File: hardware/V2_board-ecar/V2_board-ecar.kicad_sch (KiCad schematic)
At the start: 80 parts, among them IC1 ATMEGA8A-P, J1 2x BATT IN, J10 24V, J11 18V, J12 5V, J13 Analog-in-3 - 30to5 (batt), J14 Screw_Terminal_01x03, J15 Gas Pedal, J2 2x 24V filtered, J3 ST 2x GND, J4 ST 2x GND, J5 IGBT, J6 LED ~3,2V 20mA, J7 Analog-in-2 0-5V, J8 2x Mosfet OUT, J9 BATT, K1 LEG-5, P1 ISP, Q1 IRFZ24N, Q2 IRFZ24N, Q3 BC547, Q4 BC547, U1 LM2576T-5, U2 LM7818CT, U4 TC429

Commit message: pcb: Add 2x switch input, split into 3 sheets, remove mosfet output
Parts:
- removed BZ1: Buzzer, symbol Device:Buzzer
- removed C1, C2: 2200uf, symbol Device:C_Polarized
- removed C10: 100nF, ~, symbol treiber-rescue:C
- removed C11: 100n, ~, symbol treiber-rescue:C
- removed C12: 10uF, ~, symbol treiber-rescue:C
- removed C15: 10u, symbol Device:C
- removed C16, C19, C3: 100n, symbol Device:C
- removed C17: 100uF, ~, symbol treiber-rescue:C
- removed C4: 1000u, symbol Device:C_Polarized
- removed C5: 100u, symbol Device:C_Polarized
- removed C9: 330nF, ~, symbol treiber-rescue:C
- removed D1, D10, D11, D12, D13, D14, D15, D4: D, symbol Device:D
- removed D17, D7, D9: 5V1, symbol Device:D_Zener
- removed D2: TVS 26V (starts 31V), Diode_THT:D_DO-201AE_P15.24mm_Horizontal, symbol Diode:1.5KExxCA
- removed D3: 1N5822, Diode_THT:D_DO-201AD_P15.24mm_Horizontal, symbol Diode:1N5822
- removed D5: LED 3mm green 20mA 2.5V, ~, symbol control-rescue:LED
- removed F1: 500mA, symbol Device:Fuse
- removed J1: 2x BATT IN, symbol Connector:Screw_Terminal_01x02
- removed J10: 24V, symbol Connector:Conn_01x01_Pin
- removed J11: 18V, symbol Connector:Conn_01x01_Pin
- removed J12: 5V, symbol Connector:Conn_01x01_Pin
- removed J13: Analog-in-3 - 30to5 (batt), symbol Connector:Screw_Terminal_01x02
- removed J14: Screw_Terminal_01x03, symbol Connector:Screw_Terminal_01x03
- removed J15: Gas Pedal, symbol Connector:Screw_Terminal_01x03
- removed J2: 2x 24V filtered, symbol Connector:Screw_Terminal_01x02
- removed J3, J4: ST 2x GND, symbol Connector:Screw_Terminal_01x02
- removed J5: IGBT, symbol Connector:Screw_Terminal_01x02
- removed J6: LED ~3,2V 20mA, symbol Connector:Screw_Terminal_01x02
- removed J7: Analog-in-2 0-5V, symbol Connector:Screw_Terminal_01x02
- removed J8: 2x Mosfet OUT, symbol Connector:Screw_Terminal_01x02
- removed J9: BATT, symbol Connector:Conn_01x01_Pin
- removed K1: LEG-5, Relay_THT:Relay_SPDT_SANYOU_SRD_Series_Form_C, symbol Relay:SANYOU_SRD_Form_C
- removed L2: 100u, symbol Device:L
- removed OC1: LTV-817, Package_DIP_AKL:DIP-4_W7.62mm_LongPads, symbol Optocoupler_AKL:LTV-817
- removed Q1, Q2: IRFZ24N, Package_TO_SOT_THT_AKL:TO-220-3_Vertical_GDS, symbol Transistor_MOSFET_AKL:IRFZ24N
- removed Q3, Q4: BC547, Package_TO_SOT_THT_AKL:TO-92_Inline_Wide_CBE, symbol Transistor_BJT_AKL:BC547
- removed R1, R2: 2.5, symbol Device:R
- removed R10: 150k, ~, symbol control-rescue:R
- removed R11: 30k, ~, symbol control-rescue:R
- removed R12, R13, R18: 1k, ~, symbol control-rescue:R
- removed R14, R16: 1k, symbol Device:R
- removed R15, R17: 22k, symbol Device:R
- removed R19, R21: 470, symbol Device:R
- removed R20: 100, symbol Device:R
- removed R3: nopop, symbol Device:R
- removed R5: 12k, ~, symbol treiber-rescue:R
- removed R6: 0, ~, symbol treiber-rescue:R
- removed R7: 4k7, ~, symbol treiber-rescue:R
- removed R8: 320, ~, symbol treiber-rescue:R
- removed R9: 130, ~, symbol control-rescue:R
- removed U1: LM2576T-5, Package_TO_SOT_THT:TO-220-5_Vertical, symbol Regulator_Switching:LM2576T-5
- removed U2: LM7818CT, TO-220, symbol treiber-rescue:LM7818CT
- removed U4: TC429, ~, symbol mcp1407:MCP1407
- R4: value R -> 10k
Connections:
- net LED-ext: now reaches IC1.28 ((ADC5/SCL)PC5)
- net OUT0 renamed Mosfet-fan
- net OUT1 renamed Relay-light
- net SW0 renamed Switch2
- net SW1 renamed Switch1
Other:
- added sheet Input-Output (board-ecar_IO.kicad_sch)
- added sheet Voltage-Supplies (supply.kicad_sch)
- note removed: "3A overcurrent safe"
- note removed: "7-40V"
- note removed: "Onboard Buzzer, LED"
- note removed: "Relay for Light"
- note removed: "TODO: measure gas pedal voltage-drivider resistance -> choose R high enough"
- note removed: "populate diodes depending on where load is connected"
- moved on the sheet: C6, C7, C8, IC1, P1, R4

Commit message: pcb: change to A3 sheet, re-arrange, minor optimizations
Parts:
- added BZ1: Buzzer, symbol Device:Buzzer
- added C1: 100u, symbol Device:C_Polarized
- added C10, C15, C16, C17, C18: 100n, symbol Device:C
- added C11: 10u, symbol Device:C
- added C12: 100n, ~, symbol treiber-rescue:C
- added C13: 10uF, ~, symbol treiber-rescue:C
- added C14: 100uF, ~, symbol treiber-rescue:C
- added C19, C5: 1000u, symbol Device:C_Polarized
- added C2: 330nF, ~, symbol treiber-rescue:C
- added C3: 100nF, ~, symbol treiber-rescue:C
- added C4, C9: 2200uf, symbol Device:C_Polarized
- added D1, D10, D11, D8, D9: D, symbol Device:D
- added D12, D13, D5, D6, D7: 5V1, symbol Device:D_Zener
- added D2: 1N5822, Diode_THT:D_DO-201AD_P15.24mm_Horizontal, symbol Diode:1N5822
- added D3: TVS 26V (starts 31V), Diode_THT:D_DO-201AE_P15.24mm_Horizontal, symbol Diode:1.5KExxCA
- added D4: LED 3mm green 20mA 2.5V, ~, symbol control-rescue:LED
- added F1: 500mA, symbol Device:Fuse
- added J1: 2x BATT IN, symbol Connector:Screw_Terminal_01x02
- added J10: 24V, symbol Connector:Conn_01x01_Pin
- added J11: 18V, symbol Connector:Conn_01x01_Pin
- added J12: 5V, symbol Connector:Conn_01x01_Pin
- added J13: Analog-in-2 0-5V, symbol Connector:Screw_Terminal_01x02
- added J14: IGBT, symbol Connector:Screw_Terminal_01x02
- added J15: Analog-in-3 - 30to5 (batt), symbol Connector:Screw_Terminal_01x02
- added J16: Mosfet Out (Fan), symbol Connector:Screw_Terminal_01x02
- added J17: 2x Switch (to 5V), symbol Connector:Screw_Terminal_01x02
- added J18: Relay contacts, symbol Connector:Screw_Terminal_01x03
- added J2, J4: ST 2x GND, symbol Connector:Screw_Terminal_01x02
- added J3: 2x 24V filtered, symbol Connector:Screw_Terminal_01x02
- added J5: PWM-Signal, symbol Connector:Conn_01x01_Pin
- added J6: LED ~3,2V 20mA, symbol Connector:Screw_Terminal_01x02
- added J7: Gas Pedal, symbol Connector:Screw_Terminal_01x03
- added J8: Gate, symbol Connector:Conn_01x01_Pin
- added J9: BATT, symbol Connector:Conn_01x01_Pin
- added K1: LEG-5, Relay_THT:Relay_SPDT_SANYOU_SRD_Series_Form_C, symbol Relay:SANYOU_SRD_Form_C
- added L1: 100u, symbol Device:L
- added OC1: LTV-817, Package_DIP_AKL:DIP-4_W7.62mm_LongPads, symbol Optocoupler_AKL:LTV-817
- added Q1, Q3: BC547, Package_TO_SOT_THT_AKL:TO-92_Inline_Wide_CBE, symbol Transistor_BJT_AKL:BC547
- added Q2: IRFZ24N, Package_TO_SOT_THT_AKL:TO-220-3_Vertical_GDS, symbol Transistor_MOSFET_AKL:IRFZ24N
- added R1, R3: 2.5, symbol Device:R
- added R10: 4k7, ~, symbol treiber-rescue:R
- added R11, R12, R20, R26, R27: 2k2, ~, symbol control-rescue:R
- added R13, R14: 1k, ~, symbol control-rescue:R
- added R16: 150k, ~, symbol control-rescue:R
- added R17: 30k, ~, symbol control-rescue:R
- added R18: 1k, symbol Device:R
- added R19: 22k, symbol Device:R
- added R2: nopop, symbol Device:R
- added R21, R5: 470, symbol Device:R
- added R22, R23, R24, R25: 10k, ~, symbol control-rescue:R
- added R6: 320, ~, symbol treiber-rescue:R
- added R7: 130, ~, symbol control-rescue:R
- added R8: 100, symbol Device:R
- added R9: 12k, ~, symbol treiber-rescue:R
- added U1: LM7818CT, TO-220, symbol treiber-rescue:LM7818CT
- added U2: LM2576T-5, Package_TO_SOT_THT:TO-220-5_Vertical, symbol Regulator_Switching:LM2576T-5
- added U3: TC429, ~, symbol mcp1407:MCP1407
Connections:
- net SPEED0 is gone; now on net Switch2: IC1.5 ((INT1)PD3)
- net SPEED1 is gone; now on net Switch1: IC1.4 ((INT0)PD2)
- net +5V: now also C5.1, D11.1 (K), D8.1 (K), J12.1 (Pin_1), J13.2 (Pin_2), J6.1 (Pin_1), J7.3 (Pin_3), K1.5, L1.2, U2.4 (FB)
- net BUZZER: now also BZ1.1 (+)
- net GND: now also BZ1.2 (-), C1.2, C10.2, C11.2, C12.2, C13.2, C14.2, C15.2, C16.2, C17.2, C18.2, C19.2, C2.2, C3.2, C4.2, C5.2, C9.2, D1.2 (A), D12.2 (A), D13.2 (A), D2.2 (A), D3.1 (A1), D4.2 (K), D5.2 (A), D6.2 (A), D7.2 (A), J14.2 (Pin_2), J2.1 (Pin_1), J2.2 (Pin_2), J4.1 (Pin_1), J4.2 (Pin_2), J7.1 (Pin_1), OC1.2, OC1.3, Q1.3 (E), Q2.3 (S), Q3.3 (E), R10.2, R17.2, R19.1, R22.2, R23.2, U1.2 (GND), U2.3 (GND), U2.5 (~{ON}/OFF), U3.4 (GND), U3.5 (GND)
- net LED: now also R7.2
- net LED-ext: now also R5.1
- net PWM_0: now also J5.1 (Pin_1), R6.1
- net Switch1: now also R26.2; no longer IC1.12 ((AIN0)PD6)
- net Switch2: now also R27.2; no longer IC1.13 ((AIN1)PD7)
- net analog1: now also R12.1
- net Mosfet-fan renamed Mosfet (fan)
- net Mosfet (fan): now also R18.2
- net PWM_1: no longer names the net of IC1.16 ((~{SS}/OC1B)PB2)
- net RX: no longer names the net of IC1.2 ((RXD)PD0)
- net Relay-light renamed Relay (light)
- net Relay (light): now also R21.1
- net TX: no longer names the net of IC1.3 ((TXD)PD1)
- net analog0 renamed analog0 (gas)
- net analog0 (gas): now also R11.1
- net analog2-30V renamed analog2 (30V Batt)
- net analog2 (30V Batt): now also R20.2
- new net: J15.1 (Pin_1), R16.1
- new net: C16.1, D7.1 (K), R16.2, R17.1, R20.1
- new net: F1.2, R1.1, R2.1
- new net: D4.1 (A), R7.1
- new net: J14.1 (Pin_1), J8.1 (Pin_1), U3.6 (OUT), U3.7 (OUT)
- new net: D10.2 (A), D8.2 (A), D9.2 (A), J16.1 (Pin_1), Q2.2 (D)
- new net: C11.1, D5.1 (K), R11.2, R13.2
- new net: J13.1 (Pin_1), R14.1
- new net: C15.1, D6.1 (K), R12.2, R14.2
- new net: C18.1, D13.1 (K), R25.2, R27.1
- new net: Q1.1 (C), R8.2
- new net: Q1.2 (B), R5.2
- new net: Q3.2 (B), R21.2
- new net: R1.2, R3.1
- new net: Q2.1 (G), R18.1, R19.2
- new net: J7.2 (Pin_2), R13.1
- new net: J6.2 (Pin_2), R8.1
- new net: J17.1 (Pin_1), R22.1, R24.1
- new net: J17.2 (Pin_2), R23.1, R25.1
- new net: J18.1 (Pin_1), K1.4
- new net: J18.2 (Pin_2), K1.1
- new net: J18.3 (Pin_3), K1.3
- new net: D11.2 (A), K1.2, Q3.1 (C)
- new net: C17.1, D12.1 (K), R24.2, R26.1
- new net: OC1.1, R6.2
- new net: OC1.4, R10.1, R9.2, U3.2 (INPUT)
- new net: D2.1 (K), L1.1, U2.2 (OUT)
- new net +18V: C12.1, C13.1, C14.1, C19.1, C3.1, J11.1 (Pin_1), R9.1, U1.3 (OUT), U3.1 (Vdd), U3.8 (Vdd)
- new net +24V filtered: C1.1, C10.1, C2.1, C4.1, C9.1, D1.1 (K), D3.2 (A2), D9.1 (K), J10.1 (Pin_1), J15.2 (Pin_2), J16.2 (Pin_2), J3.1 (Pin_1), J3.2 (Pin_2), R2.2, R3.2, U1.1 (IN), U2.1 (VIN)
- new net +BATT: D10.1 (K), F1.1, J1.1 (Pin_1), J1.2 (Pin_2), J9.1 (Pin_1)
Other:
- removed sheet Input-Output
- removed sheet Voltage-Supplies
- note added: "18V Supply (linear regulator)"
- note added: "18V needed for mosfet driver"
- note added: "24V Supply voltage filter"
- note added: "2x Digital input (Switches to 5V)"
- note added: "3A overcurrent safe"
- note added: "5V Supply (buck converter)"
- note added: "7-40V"
- note added: "ADC Battery voltage"
- note added: "ADC Gas pedal"
- note added: "ADC Reserve"
- note added: "Filter 50V peaks on battery voltage each pwm cycle"
- note added: "Mosfet driver for IGBT"
- note added: "Mosfet out (cooling Fan)"
- note added: "Onboard Buzzer and LED"
- note added: "Relay for Light"
- note added: "TODO: measure gas pedal voltage-drivider resistance -> choose R high enough"
- note added: "external LED"
- note added: "populate diodes depending on where load is connected"
- note added: "test pins supplies"
- note removed: "Shopping list: 5V Voltage regulator LM2576T-5 Diode 1N5822 100uH >3A inductor"
- moved on the sheet: C6, C7, C8, IC1, P1, R4

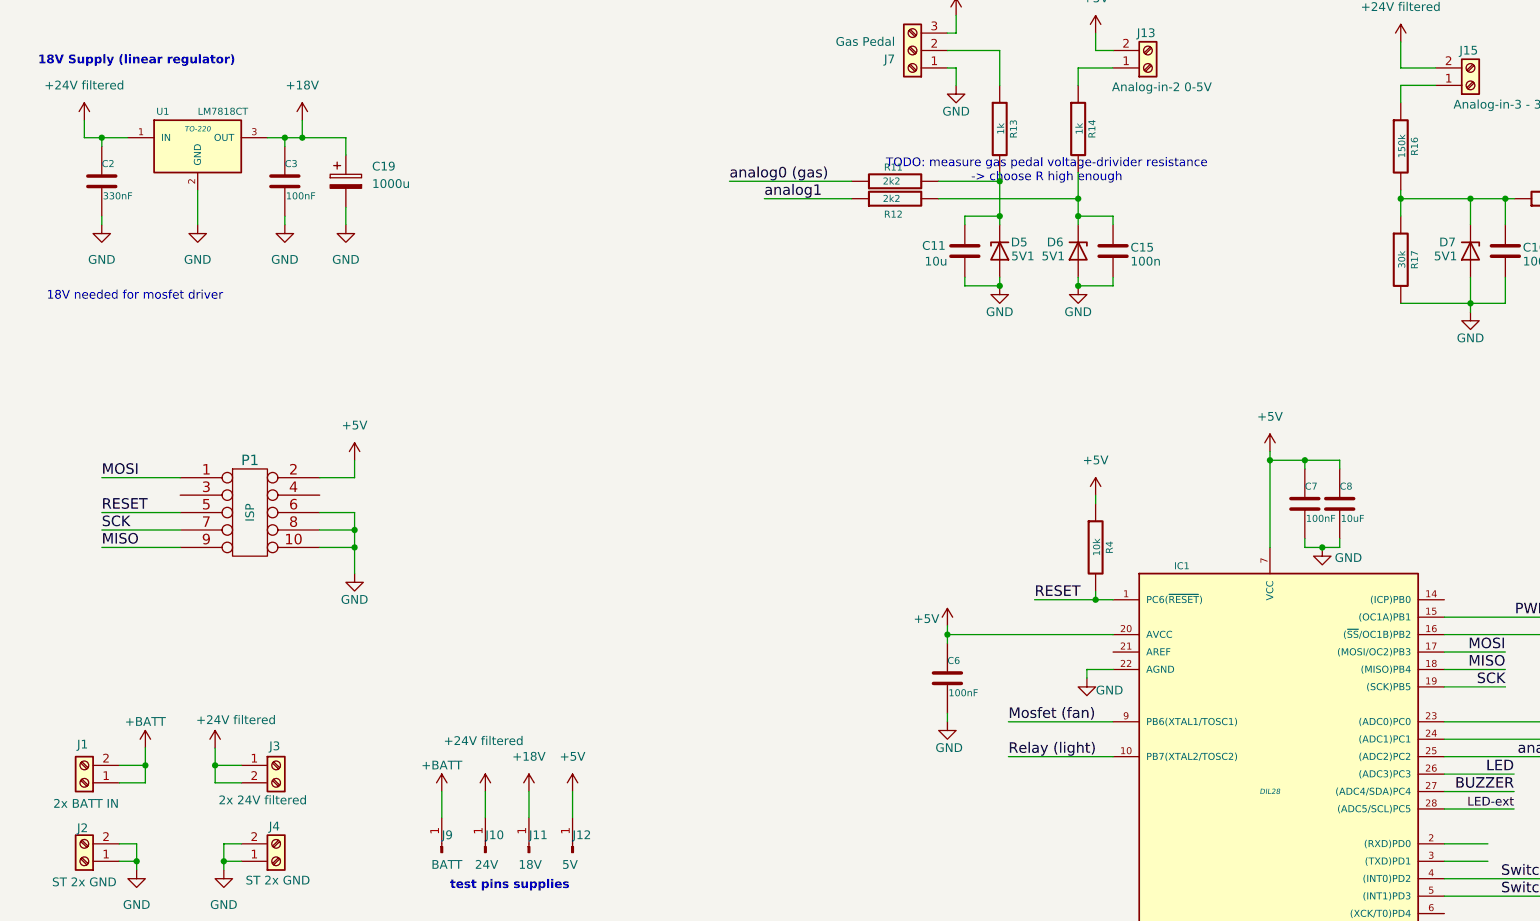
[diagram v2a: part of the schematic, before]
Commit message: pcb: Assign footprints
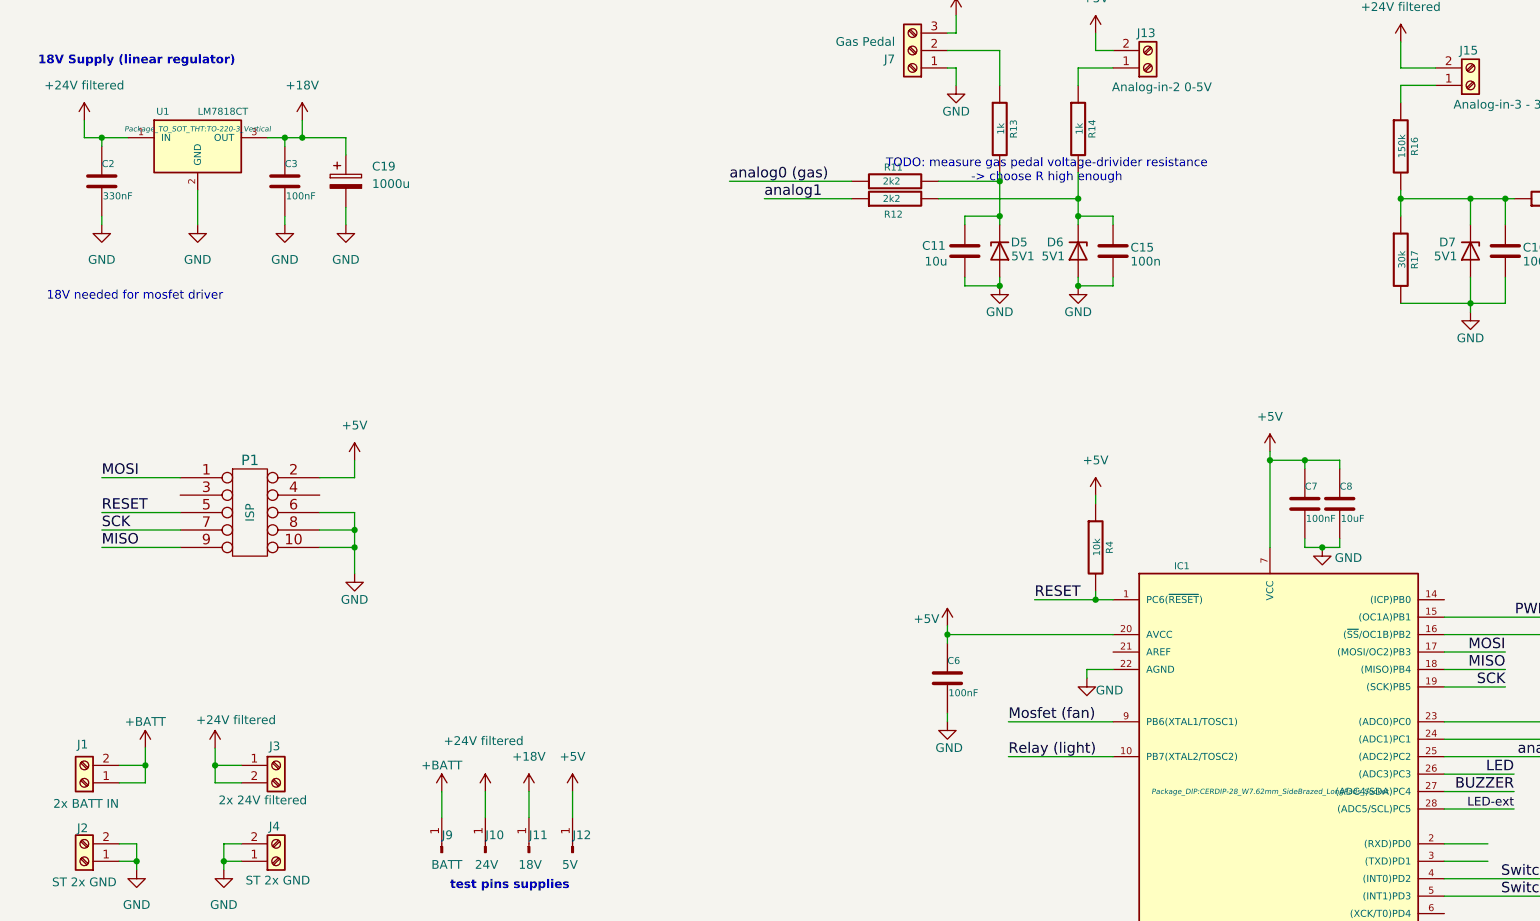
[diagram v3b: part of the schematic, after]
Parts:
- BZ1: footprint (none) -> Buzzer_Beeper:MagneticBuzzer_ProSignal_ABT-410-RC
- C1: footprint (none) -> Capacitor_THT:CP_Radial_D8.0mm_P5.00mm
- C10, C15, C16, C17, C18: footprint (none) -> Capacitor_THT:C_Disc_D7.0mm_W2.5mm_P5.00mm
- C11: footprint (none) -> Capacitor_THT:CP_Radial_D5.0mm_P2.50mm
- C12, C3, C6, C7: footprint ~ -> Capacitor_THT:C_Disc_D7.0mm_W2.5mm_P5.00mm
- C13, C8: footprint ~ -> Capacitor_THT:CP_Radial_D5.0mm_P2.50mm
- C14: footprint ~ -> Capacitor_THT:CP_Radial_D8.0mm_P5.00mm
- C19, C5: footprint (none) -> Capacitor_THT:CP_Radial_D10.0mm_P5.00mm
- C2: footprint ~ -> Capacitor_THT:C_Disc_D8.0mm_W5.0mm_P5.00mm
- C4, C9: footprint (none) -> Capacitor_THT:CP_Radial_D18.0mm_P7.50mm
- D1, D10, D11, D8, D9: footprint (none) -> Diode_THT:D_T-1_P12.70mm_Horizontal
- D12, D13, D5, D6, D7: footprint (none) -> Diode_THT:D_A-405_P10.16mm_Horizontal
- D4: footprint ~ -> LED_THT:LED_D3.0mm_Clear
- F1: footprint (none) -> Fuse:Fuseholder_Cylinder-5x20mm_Stelvio-Kontek_PTF78_Horizontal_Open
- IC1: footprint DIL28 -> Package_DIP:CERDIP-28_W7.62mm_SideBrazed_LongPads_Socket
- J1, J13, J14, J15, J16, J17, J2, J3, J4, J6: footprint (none) -> TerminalBlock:TerminalBlock_bornier-2_P5.08mm
- J10, J11, J12, J5, J8, J9: footprint (none) -> Connector_PinHeader_1.00mm:PinHeader_1x01_P1.00mm_Vertical
- J18, J7: footprint (none) -> TerminalBlock:TerminalBlock_bornier-3_P5.08mm
- L1: footprint (none) -> Inductor_THT:L_Radial_D8.7mm_P5.00mm_Fastron_07HCP
- OC1: footprint Package_DIP_AKL:DIP-4_W7.62mm_LongPads -> Package_DIP:DIP-4_W10.16mm_LongPads
- P1: footprint ~ -> Connector_IDC:IDC-Header_2x05_P2.54mm_Vertical
- Q1, Q3: footprint Package_TO_SOT_THT_AKL:TO-92_Inline_Wide_CBE -> Package_TO_SOT_THT:TO-92L
- Q2: footprint Package_TO_SOT_THT_AKL:TO-220-3_Vertical_GDS -> Package_TO_SOT_THT:TO-220-3_Vertical
- R1, R2, R3: footprint (none) -> Resistor_THT:R_Axial_DIN0922_L20.0mm_D9.0mm_P25.40mm_Horizontal
- R10, R11, R12, R13, R14, R16, R17, R20, R22, R23, R24, R25, R26, R27, R4, R6, R7, R9: footprint ~ -> Resistor_THT:R_Axial_DIN0207_L6.3mm_D2.5mm_P10.16mm_Horizontal
- R18, R19, R21, R5, R8: footprint (none) -> Resistor_THT:R_Axial_DIN0207_L6.3mm_D2.5mm_P10.16mm_Horizontal
- U1: footprint TO-220 -> Package_TO_SOT_THT:TO-220-3_Vertical
- U3: footprint ~ -> Package_DIP:DIP-8_W7.62mm_Socket_LongPads
